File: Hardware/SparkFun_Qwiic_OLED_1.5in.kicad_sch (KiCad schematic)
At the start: 39 parts, among them J1 Qwiic_RA, J2 Qwiic_RA, J4 Conn_01x24_FPC, J5 Conn_01x07, U2 WEO128128ASAP3N00000, U5 AP3012

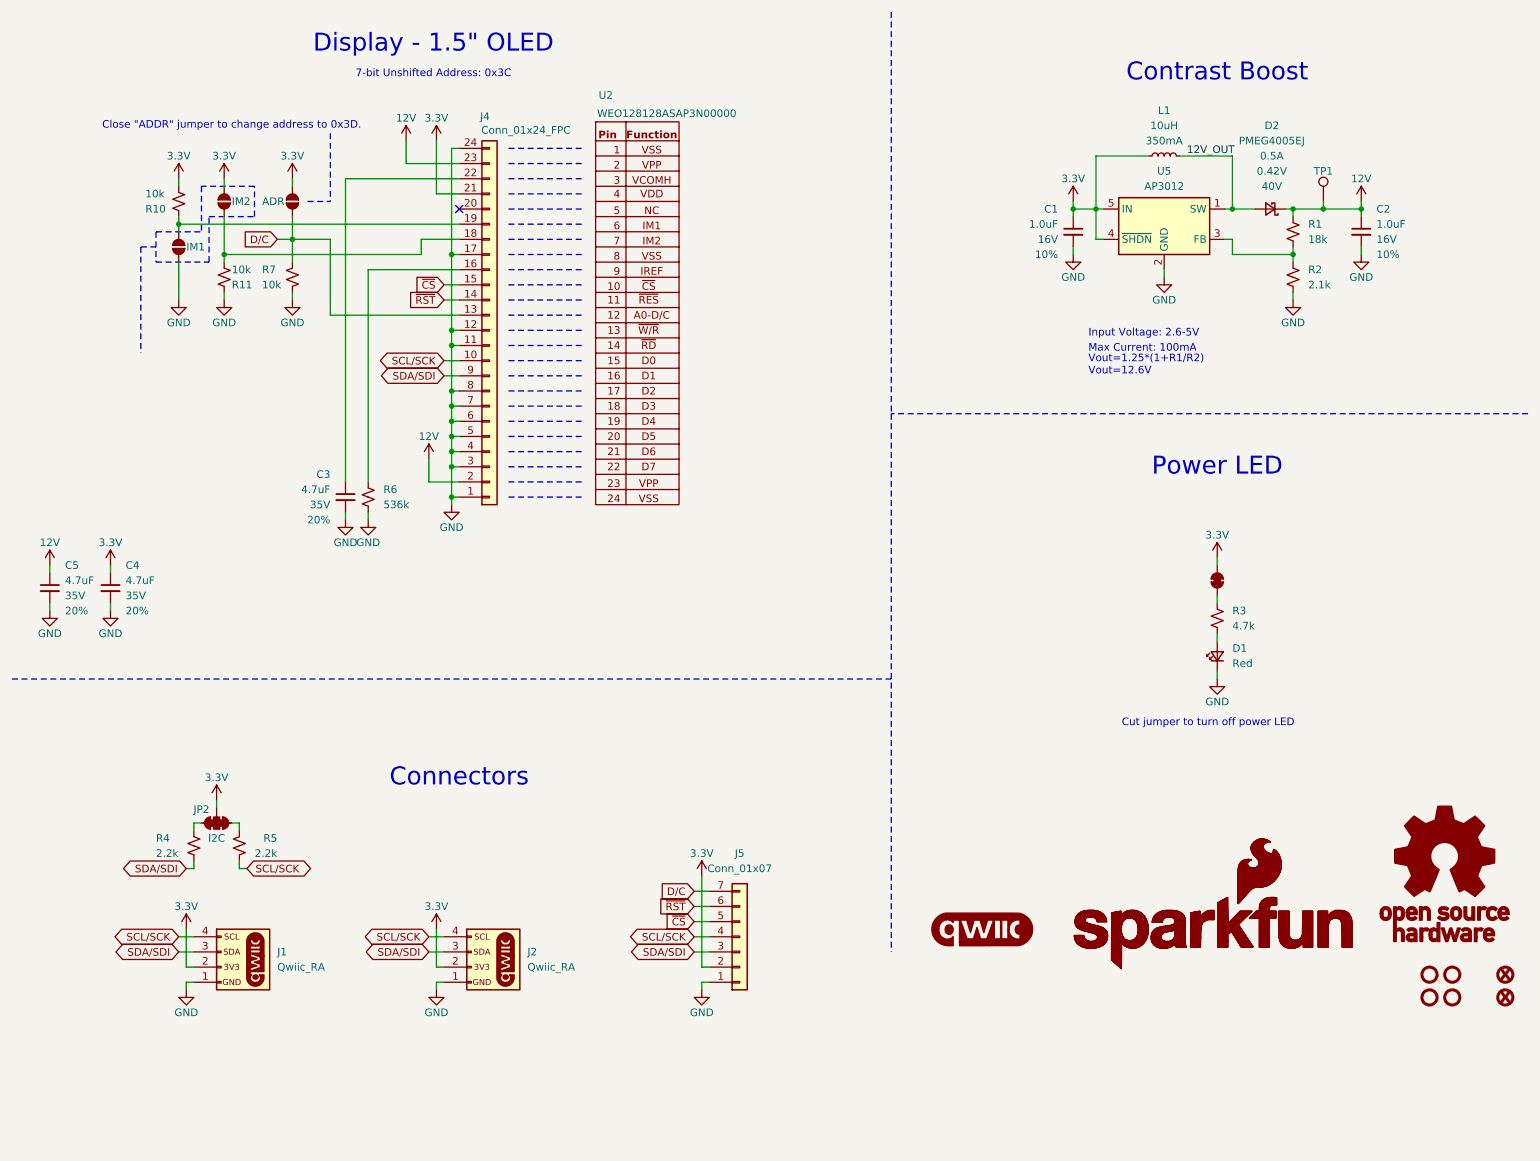
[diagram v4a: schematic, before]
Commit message: Cleans up schematic, adds table to silk for interface settings
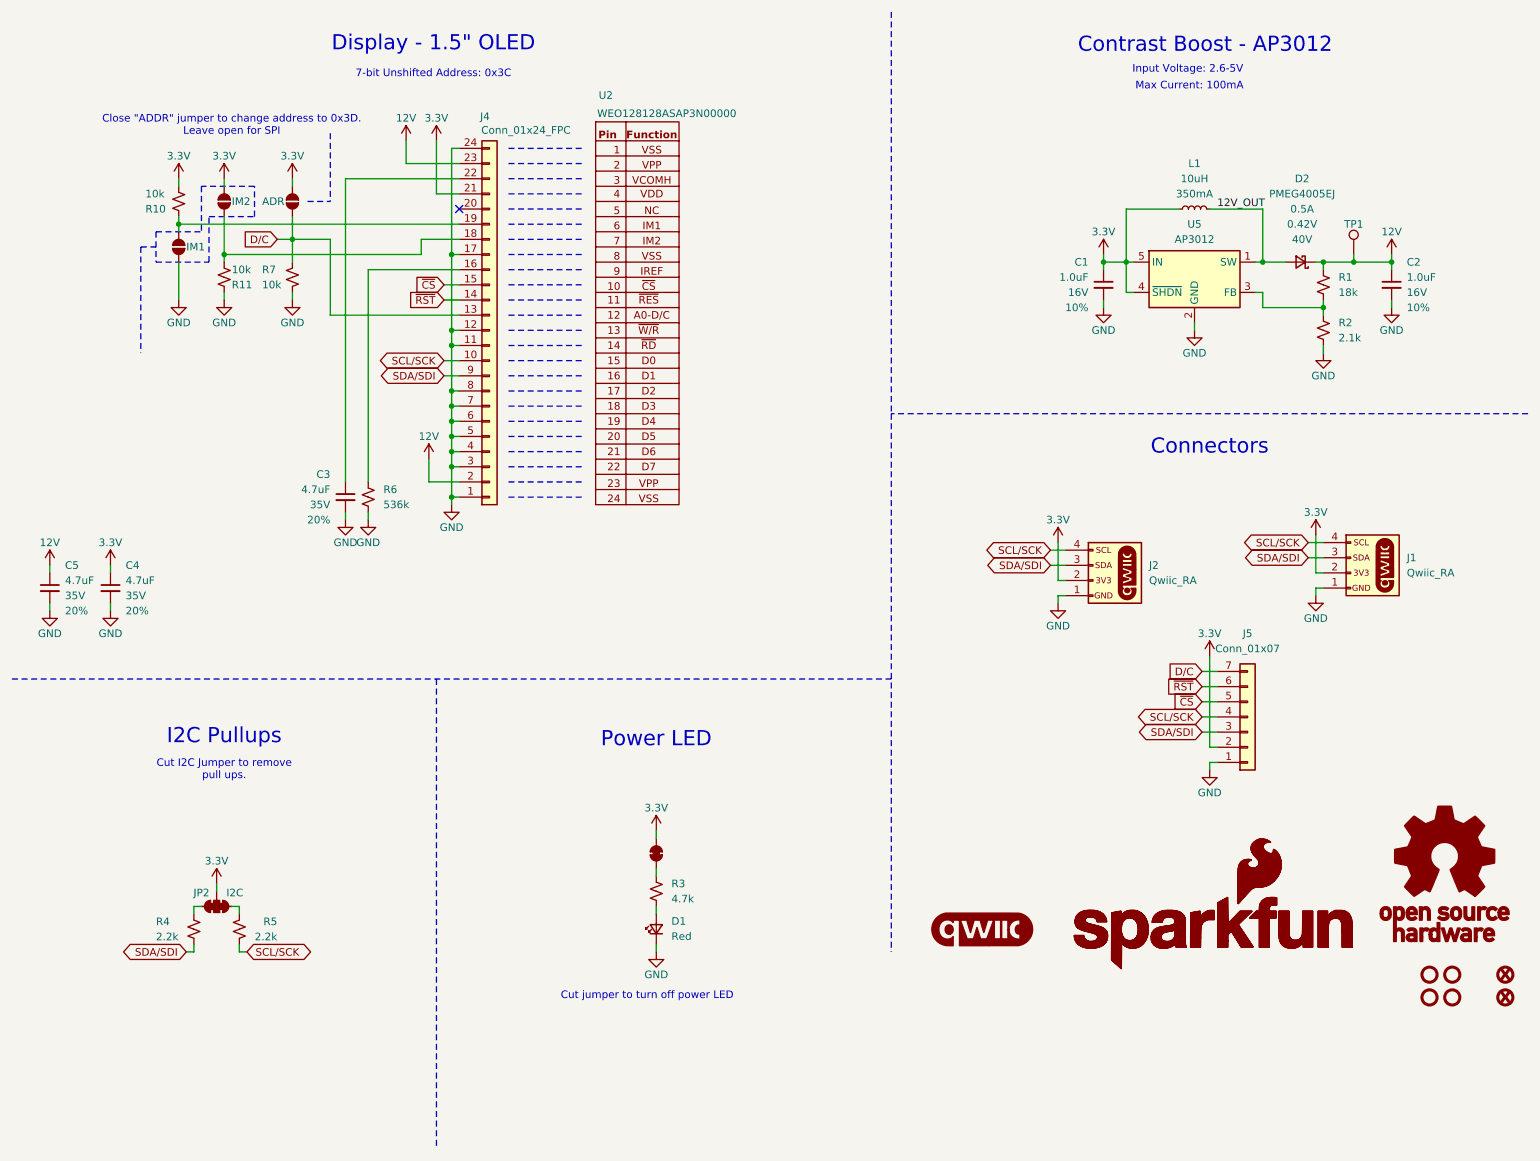
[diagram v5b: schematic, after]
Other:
- note added: "Close "ADDR" jumper to change address to 0x3D. Leave open for SPI"
- note added: "Contrast Boost - AP3012"
- note added: "Cut I2C Jumper to remove pull ups."
- note added: "I2C Pullups"
- note removed: "Close "ADDR" jumper to change address to 0x3D."
- note removed: "Contrast Boost"
- note removed: "Vout=1.25*(1+R1/R2) Vout=12.6V"
- moved on the sheet: C1, C2, D1, D2, J1, J2, J5, JP2, L1, R1, R2, R3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

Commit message: Fixes some text on the LED jumper
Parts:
- JP1: value ~ -> LED
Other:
- note added: "Cut "LED" jumper to turn off power LED"
- note removed: "Cut jumper to turn off power LED"
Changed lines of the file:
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@@
 		)
 	)
-	(text "Cut jumper to turn off power LED"
+	(text "Cut \"LED\" jumper to turn off power LED"
 		(exclude_from_sim no)
-		(at 104.648 179.578 0)
+		(at 104.902 140.97 0)
 		(effects
 			(font
@@
 		(dnp no)
 		(property "Reference" "JP1"
-			(at 123.19 154.3049 90)
+			(at 122.682 153.67 90)
 			(effects
 				(font
@@
 				)
 				(justify right)
-				(hide yes)
 			)
 		)
-		(property "Value" "~"
-			(at 122.428 155.194 90)
+		(property "Value" "LED"
+			(at 122.682 155.956 90)
 			(effects
 				(font

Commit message: Adds "I2C" to address in schematic, removes stub
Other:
- note added: "7-bit Unshifted I²C Address: 0x3C"
- note removed: "7-bit Unshifted Address: 0x3C"
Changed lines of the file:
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@@
 		)
 	)
-	(text "7-bit Unshifted Address: 0x3C"
+	(text "7-bit Unshifted I²C Address: 0x3C"
 		(exclude_from_sim no)
 		(at 83.312 24.384 0)

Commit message: Replaces the 536k part with a 549k part
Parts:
- removed R6: 536k, SparkFun-Resistor:R_0603_1608Metric, symbol SparkFun-Resistor:536k_0603
- added R6: 549k, SparkFun-Resistor:R_0603_1608Metric, symbol SparkFun-Resistor:549k_0603
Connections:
- net GND: now also R6.1
- net at J4.16 (Pin_16): now also R6.2
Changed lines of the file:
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@@
 	)
 	(symbol
-		(lib_id "SparkFun-Resistor:536k_0603")
-		(at 72.39 95.25 90)
-		(unit 1)
-		(exclude_from_sim no)
-		(in_bom yes)
-		(on_board yes)
-		(dnp no)
-		(fields_autoplaced yes)
-		(property "Reference" "R6"
-			(at 74.93 93.9799 90)
-			(effects
-				(font
-					(size 1.27 1.27)
-				)
-				(justify right)
-			)
-		)
-		(property "Value" "536k"
-			(at 74.93 96.5199 90)
-			(effects
-				(font
-					(size 1.27 1.27)
-				)
-				(justify right)
-			)
-		)
-		(property "Footprint" "SparkFun-Resistor:R_0603_1608Metric"
-			(at 76.962 95.25 0)
-			(effects
-				(font
-					(size 1.27 1.27)
-				)
-				(hide yes)
-			)
-		)
-		(property "Datasheet" "https://www.vishay.com/docs/20035/dcrcwe3.pdf"
-			(at 81.28 95.25 0)
-			(effects
-				(font
-					(size 1.27 1.27)
-				)
-				(hide yes)
-			)
-		)
-		(property "Description" "Resistor"
-			(at 83.82 95.25 0)
-			(effects
-				(font
-					(size 1.27 1.27)
-				)
-				(hide yes)
-			)
-		)
-		(property "PROD_ID" "RES-26754"
-			(at 79.248 95.25 0)
-			(effects
-				(font
-					(size 1.27 1.27)
-				)
-				(hide yes)
-			)
-		)
-		(pin "2"
-		)
-		(pin "1"
-		)
-		(instances
-			(project ""
-				(path "/e3dd3ae4-244d-4cba-9cca-5d2abf83f29a"
-					(reference "R6")
-					(unit 1)
-				)
-			)
-		)
-	)
-	(symbol
 		(lib_id "SparkFun-Resistor:2.1k_0603")
 		(at 232.41 67.31 90)
@@
 					(unit 1)
 				)
+			)
+		)
+	)
+	(symbol
+		(lib_id "SparkFun-Resistor:549k_0603")
+		(at 72.39 95.25 90)
+		(unit 1)
+		(exclude_from_sim no)
+		(in_bom yes)
+		(on_board yes)
+		(dnp no)
+		(fields_autoplaced yes)
+		(property "Reference" "R6"
+			(at 74.93 93.9799 90)
+			(effects
+				(font
+					(size 1.27 1.27)
+				)
+				(justify right)
+			)
+		)
+		(property "Value" "549k"
+			(at 74.93 96.5199 90)
+			(effects
+				(font
+					(size 1.27 1.27)
+				)
+				(justify right)
+			)
+		)
+		(property "Footprint" "SparkFun-Resistor:R_0603_1608Metric"
+			(at 76.962 95.25 0)
+			(effects
+				(font
+					(size 1.27 1.27)
+				)
+				(hide yes)
+			)
+		)
+		(property "Datasheet" "https://www.vishay.com/docs/20035/dcrcwe3.pdf"
+			(at 81.28 95.25 0)
+			(effects
+				(font
+					(size 1.27 1.27)
+				)
+				(hide yes)
+			)
+		)
+		(property "Description" "549kΩ 100mW 75V ±25ppm/℃ ±0.1% 0603"
+			(at 83.82 95.25 0)
+			(effects
+				(font
+					(size 1.27 1.27)
+				)
+				(hide yes)
+			)
+		)
+		(property "PROD_ID" "RES-26754"
+			(at 79.248 95.25 0)
+			(effects
+				(font
+					(size 1.27 1.27)
+				)
+				(hide yes)
+			)
+		)
+		(pin "2"
+		)
+		(pin "1"
+		)
+		(instances
+			(project ""
+				(path "/e3dd3ae4-244d-4cba-9cca-5d2abf83f29a"
+					(reference "R6")
+					(unit 1)
+				)
